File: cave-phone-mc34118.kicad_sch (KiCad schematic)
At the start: 68 parts, among them J1 Conn_01x02_Female, SW1 L-KLS7-SK02-12E12-EG7, SW2 SW_SPST, SW3 L-KLS7-SK02-12E12-EG7, SW4 SW_SPST, T1 SM-LP-5001, U2 MC34118, U3 MC34119G-SO8

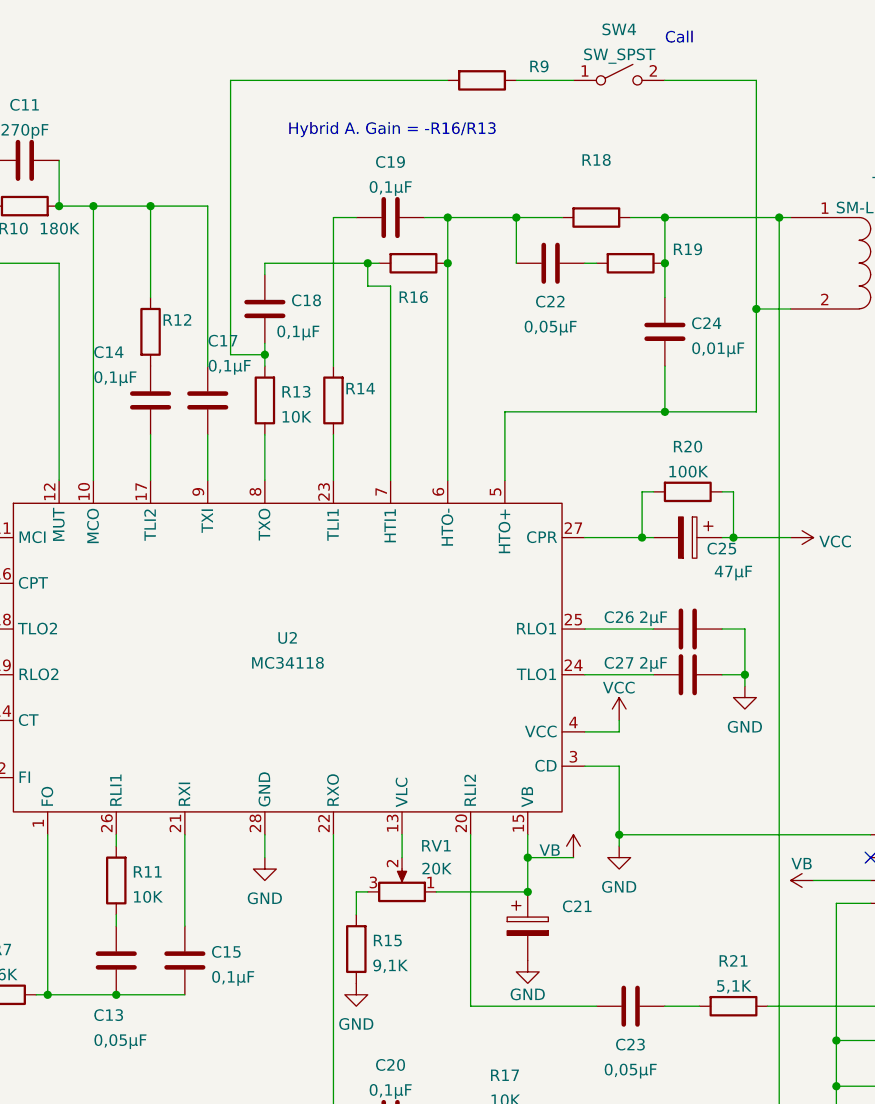
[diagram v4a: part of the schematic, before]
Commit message: WiP: New PCB (0805 SMDs)
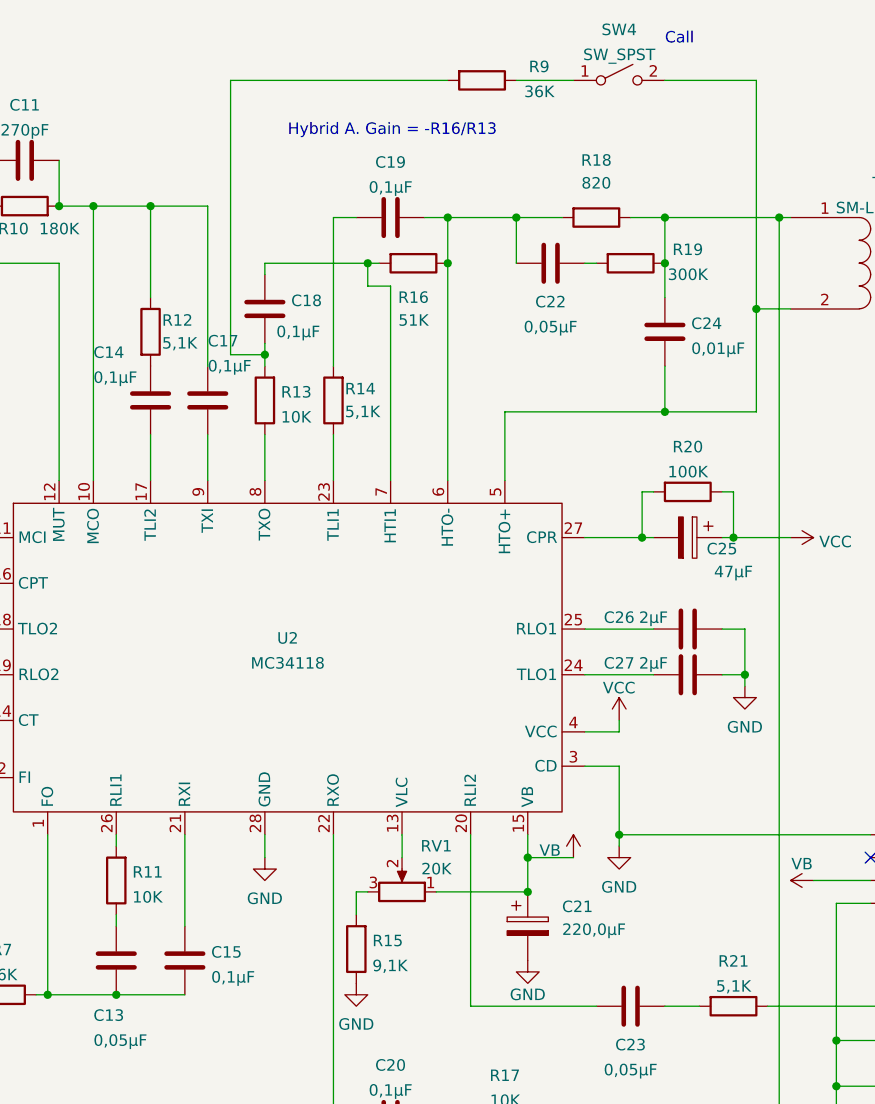
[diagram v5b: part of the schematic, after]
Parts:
- C1, C10, C11, C12, C13, C14, C15, C17, C18, C19, C20, C22, C23, C24, C26, C27, C28, C4, C6, C7, C9: footprint Capacitor_SMD:C_0603_1608Metric -> (none)
- C2, C25, C3, C8: footprint Capacitor_Tantalum_SMD:CP_EIA-3528-21_Kemet-B -> (none)
- C21: value (none) -> 220,0µF; footprint Capacitor_Tantalum_SMD:CP_EIA-3528-21_Kemet-B -> (none)
- C5: footprint Capacitor_SMD:C_0805_2012Metric -> (none)
- R1, R10, R11, R13, R15, R17, R2, R20, R21, R22, R23, R3, R4, R5, R6, R7, R8: footprint Resistor_SMD:R_0603_1608Metric -> (none)
- R12, R14: value (none) -> 5,1K; footprint Resistor_SMD:R_0603_1608Metric -> (none)
- R16: value (none) -> 51K; footprint Resistor_SMD:R_0603_1608Metric -> (none)
- R18: value (none) -> 820; footprint Resistor_SMD:R_0603_1608Metric -> (none)
- R19: value (none) -> 300K; footprint Resistor_SMD:R_0603_1608Metric -> (none)
- R9: value (none) -> 36K; footprint Resistor_SMD:R_0603_1608Metric -> (none)

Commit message: WiP: New PCB
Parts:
- C1, C11, C12, C14, C15, C17, C18, C19, C20, C24, C28, C6, C7: footprint (none) -> Capacitor_SMD:C_0805_2012Metric_Pad1.18x1.45mm_HandSolder
- C10, C26, C27, C9: value 2µF -> (none); footprint (none) -> Capacitor_SMD:C_0805_2012Metric_Pad1.18x1.45mm_HandSolder
- C13, C22, C23: value 0,05µF -> (none); footprint (none) -> Capacitor_SMD:C_0805_2012Metric_Pad1.18x1.45mm_HandSolder
- C2: value 20µF -> (none)
- C29: footprint Capacitor_SMD:CP_Elec_10x10.5 -> (none)
- C3: value 5,0µF -> (none)
- C4: value 0,02µF -> (none); footprint (none) -> Capacitor_SMD:C_0805_2012Metric_Pad1.18x1.45mm_HandSolder
- C5: value 0,2µF -> (none); footprint (none) -> Capacitor_SMD:C_0805_2012Metric_Pad1.18x1.45mm_HandSolder
- C8: footprint (none) -> Capacitor_Tantalum_SMD:CP_EIA-3528-21_Kemet-B_Pad1.50x2.35mm_HandSolder
- J1: footprint Connector_Molex:Molex_SPOX_5267-02A_1x02_P2.50mm_Vertical -> (none)
- R23: value 5K -> (none)
- SW1: value L-KLS7-SK02-12E12-EG7 -> (none)
- SW2, SW4: footprint Button_Switch_SMD:SW_Push_1P1T_NO_6x6mm_H9.5mm -> (none)
